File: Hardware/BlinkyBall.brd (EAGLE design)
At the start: 3 parts, among them IC3 TINY13-20SSU

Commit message: Adjust for LED
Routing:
- net S$13: track 1.59 -> 0.00 mm
- net S$11: track 19.2 -> 17.9 mm
- net S$8: track 0.63 -> 1.43 mm
- net S$6: track 0.79 -> 1.43 mm
- net S$2: track 5.71 -> 6.35 mm
- net N$28: track 8.24 -> 7.73 mm
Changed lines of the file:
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@@
 <text x="14.605" y="9.2075" size="1.6764" layer="1" rot="R90">9/12</text>
 <rectangle x1="7.77875" y1="15.5575" x2="10.31875" y2="18.0975" layer="1"/>
-<rectangle x1="11.58875" y1="5.08" x2="14.12875" y2="7.62" layer="1"/>
+<rectangle x1="11.58875" y1="5.23875" x2="14.12875" y2="7.6835" layer="1"/>
 <rectangle x1="11.58875" y1="16.1925" x2="14.605" y2="17.78" layer="1"/>
 <rectangle x1="11.58875" y1="14.12875" x2="14.605" y2="15.71625" layer="1"/>
 <text x="16.8275" y="11.7475" size="1.778" layer="1" rot="R90">SYN</text>
 <text x="18.7325" y="3.33375" size="1.778" layer="1" rot="R90">man</text>
-<text x="4.445" y="7.62" size="1.27" layer="1" rot="R270">blinky</text>
-<text x="7.62" y="4.445" size="1.27" layer="1" rot="R180">all</text>
-<text x="14.2875" y="4.445" size="1.016" layer="1" rot="R180">4.1</text>
+<text x="4.28625" y="8.09625" size="1.27" layer="1" rot="R270">blinky</text>
+<text x="7.3025" y="4.92125" size="1.27" layer="1" rot="R180">all</text>
+<text x="14.44625" y="4.60375" size="1.016" layer="1" rot="R180">4.1</text>
 <text x="18.25625" y="12.7" size="1.778" layer="1" rot="R90">shop</text>
-<text x="17.30375" y="2.2225" size="1.778" layer="1" rot="R90">data</text>
+<text x="17.30375" y="2.8575" size="1.778" layer="1" rot="R90">data</text>
 <text x="11.1125" y="10.63625" size="1.27" layer="1" rot="R180">Padi</text>
 <text x="11.43" y="9.36625" size="1.27" layer="1" rot="R180">wan</text>
@@
 <signal name="N$28">
 <contactref element="R3" pad="1"/>
-<wire x1="9.36625" y1="2.425" x2="9.2075" y2="2.54" width="0.4064" layer="1"/>
-<wire x1="9.2075" y1="2.54" x2="3.33375" y2="2.54" width="0.6096" layer="1"/>
-<wire x1="3.33375" y1="2.54" x2="3.33375" y2="4.715" width="0.6096" layer="1"/>
+<wire x1="9.36625" y1="3.01625" x2="3.33375" y2="3.01625" width="0.6096" layer="1"/>
+<wire x1="3.33375" y1="3.01625" x2="3.33375" y2="4.715" width="0.6096" layer="1"/>
 </signal>
 <signal name="N$30">
@@
 <wire x1="11.89625" y1="6.71225" x2="11.89625" y2="6.82625" width="0.4064" layer="1"/>
 <wire x1="11.89625" y1="6.82625" x2="11.90625" y2="6.82625" width="0.6096" layer="1"/>
-<wire x1="11.90625" y1="6.82625" x2="11.90625" y2="5.715" width="0.6096" layer="1"/>
+<wire x1="11.90625" y1="6.82625" x2="11.90625" y2="5.588" width="0.6096" layer="1"/>
 </signal>
 <signal name="N$15">
@@
 </signal>
 <signal name="S$2">
-<wire x1="10.63625" y1="4.445" x2="11.43" y2="4.445" width="0.6096" layer="1"/>
+<wire x1="10.63625" y1="4.445" x2="12.065" y2="4.445" width="0.6096" layer="1"/>
 <wire x1="9.36625" y1="17.78" x2="14.2875" y2="17.78" width="0.6096" layer="1"/>
 </signal>
@@
 <signal name="S$11">
 <wire x1="11.90625" y1="13.49375" x2="11.90625" y2="8.5725" width="0.6096" layer="1"/>
-<wire x1="15.08125" y1="8.5725" x2="15.08125" y2="2.54" width="0.6096" layer="1"/>
-<wire x1="15.08125" y1="2.54" x2="10.63625" y2="2.54" width="0.6096" layer="1"/>
+<wire x1="15.08125" y1="8.5725" x2="14.9225" y2="3.01625" width="0.6096" layer="1"/>
+<wire x1="14.9225" y1="3.01625" x2="11.27125" y2="3.01625" width="0.6096" layer="1"/>
 <wire x1="11.90625" y1="8.5725" x2="15.08125" y2="8.5725" width="0.6096" layer="1"/>
-<wire x1="10.63625" y1="2.54" x2="10.63625" y2="3.175" width="0.6096" layer="1"/>
+<wire x1="11.27125" y1="3.01625" x2="10.63625" y2="3.01625" width="0.6096" layer="1"/>
 </signal>
 <signal name="S$12">
@@
 </signal>
 <signal name="S$8">
-<wire x1="9.2075" y1="4.445" x2="8.5725" y2="4.445" width="0.6096" layer="1"/>
-</signal>
-<signal name="S$13">
-<wire x1="9.36625" y1="2.54" x2="9.36625" y2="3.33375" width="0.6096" layer="1"/>
-<wire x1="9.36625" y1="3.33375" x2="8.5725" y2="3.33375" width="0.6096" layer="1"/>
+<wire x1="9.2075" y1="4.445" x2="7.77875" y2="4.445" width="0.6096" layer="1"/>
 </signal>
 <signal name="S$1">
@@
 </signal>
 <signal name="S$6">
-<wire x1="10.63625" y1="3.33375" x2="11.43" y2="3.33375" width="0.6096" layer="1"/>
+<wire x1="10.63625" y1="3.01625" x2="12.065" y2="3.01625" width="0.6096" layer="1"/>
 </signal>
 <signal name="S$9">

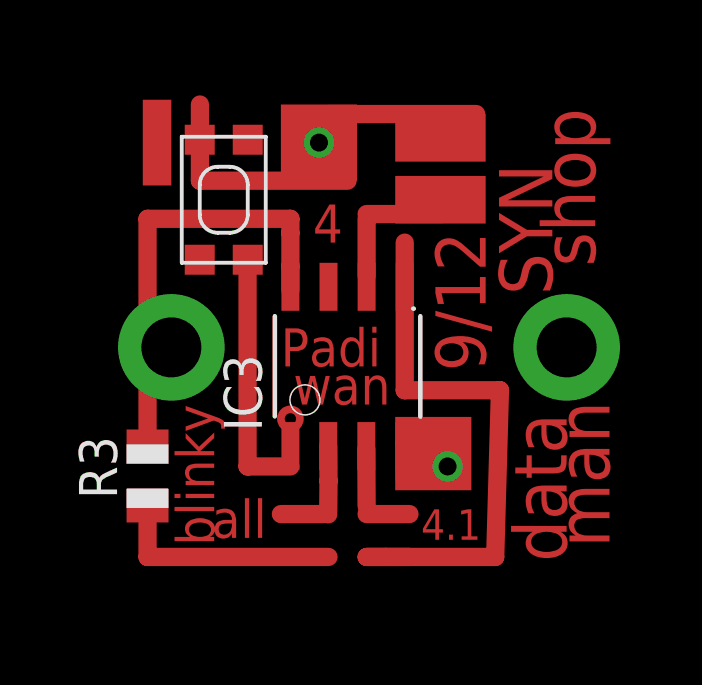
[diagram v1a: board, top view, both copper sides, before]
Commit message: Adjusting Layout, v4.2
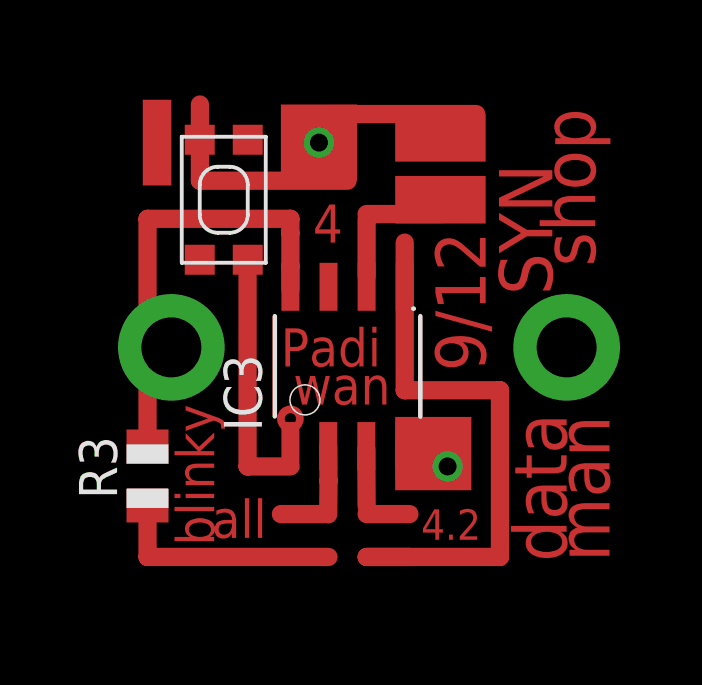
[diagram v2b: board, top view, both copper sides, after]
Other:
- board text added: "4.2"
- board text removed: "4.1"
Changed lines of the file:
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@@
 <rectangle x1="11.58875" y1="14.12875" x2="14.605" y2="15.71625" layer="1"/>
 <text x="16.8275" y="11.7475" size="1.778" layer="1" rot="R90">SYN</text>
-<text x="18.7325" y="3.33375" size="1.778" layer="1" rot="R90">man</text>
+<text x="18.7325" y="2.8575" size="1.778" layer="1" rot="R90">man</text>
 <text x="4.28625" y="8.09625" size="1.27" layer="1" rot="R270">blinky</text>
 <text x="7.3025" y="4.92125" size="1.27" layer="1" rot="R180">all</text>
-<text x="14.44625" y="4.60375" size="1.016" layer="1" rot="R180">4.1</text>
+<text x="14.44625" y="4.60375" size="1.016" layer="1" rot="R180">4.2</text>
 <text x="18.25625" y="12.7" size="1.778" layer="1" rot="R90">shop</text>
 <text x="17.30375" y="2.8575" size="1.778" layer="1" rot="R90">data</text>
@@
 <signal name="S$11">
 <wire x1="11.90625" y1="13.49375" x2="11.90625" y2="8.5725" width="0.6096" layer="1"/>
-<wire x1="15.08125" y1="8.5725" x2="14.9225" y2="3.01625" width="0.6096" layer="1"/>
-<wire x1="14.9225" y1="3.01625" x2="11.27125" y2="3.01625" width="0.6096" layer="1"/>
+<wire x1="15.08125" y1="8.5725" x2="15.08125" y2="3.01625" width="0.6096" layer="1"/>
+<wire x1="15.08125" y1="3.01625" x2="10.63625" y2="3.01625" width="0.6096" layer="1"/>
 <wire x1="11.90625" y1="8.5725" x2="15.08125" y2="8.5725" width="0.6096" layer="1"/>
-<wire x1="11.27125" y1="3.01625" x2="10.63625" y2="3.01625" width="0.6096" layer="1"/>
 </signal>
 <signal name="S$12">

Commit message: Final Board Adjustments?
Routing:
- net S$2: track 6.35 -> 8.73 mm
- net S$5: track 2.54 -> 4.29 mm
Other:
- board text added: "4.3"
- board text added: "hop"
- board text removed: "4"
- board text removed: "4.2"
- board text removed: "shop"
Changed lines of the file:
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@@
 <plain>
 <circle x="8.09625" y="7.62" radius="0.3175" width="0.254" layer="1"/>
-<text x="14.605" y="9.2075" size="1.6764" layer="1" rot="R90">9/12</text>
 <rectangle x1="7.77875" y1="15.5575" x2="10.31875" y2="18.0975" layer="1"/>
 <rectangle x1="11.58875" y1="5.23875" x2="14.12875" y2="7.6835" layer="1"/>
-<rectangle x1="11.58875" y1="16.1925" x2="14.605" y2="17.78" layer="1"/>
-<rectangle x1="11.58875" y1="14.12875" x2="14.605" y2="15.71625" layer="1"/>
-<text x="16.8275" y="11.7475" size="1.778" layer="1" rot="R90">SYN</text>
 <text x="18.7325" y="2.8575" size="1.778" layer="1" rot="R90">man</text>
-<text x="4.28625" y="8.09625" size="1.27" layer="1" rot="R270">blinky</text>
-<text x="7.3025" y="4.92125" size="1.27" layer="1" rot="R180">all</text>
-<text x="14.44625" y="4.60375" size="1.016" layer="1" rot="R180">4.2</text>
-<text x="18.25625" y="12.7" size="1.778" layer="1" rot="R90">shop</text>
+<text x="4.445" y="7.3025" size="1.016" layer="1" rot="R270">blinky</text>
+<text x="6.985" y="4.7625" size="1.016" layer="1" rot="R180">all</text>
+<text x="13.81125" y="16.8275" size="1.4224" layer="1" rot="R180">4.3</text>
 <text x="17.30375" y="2.8575" size="1.778" layer="1" rot="R90">data</text>
-<text x="11.1125" y="10.63625" size="1.27" layer="1" rot="R180">Padi</text>
-<text x="11.43" y="9.36625" size="1.27" layer="1" rot="R180">wan</text>
-<text x="9.8425" y="14.76375" size="1.27" layer="1" rot="R180">4</text>
+<text x="10.95375" y="10.795" size="1.27" layer="1" rot="R180">Padi</text>
+<text x="11.27125" y="9.525" size="1.27" layer="1" rot="R180">wan</text>
 <rectangle x1="3.175" y1="15.39875" x2="4.1275" y2="18.25625" layer="1"/>
+<rectangle x1="14.44625" y1="16.1925" x2="18.89125" y2="18.0975" layer="1"/>
+<text x="13.97" y="13.49375" size="1.27" layer="1" rot="SR270">SYN</text>
+<text x="15.5575" y="12.3825" size="1.27" layer="1">hop</text>
+<text x="12.54125" y="12.85875" size="1.016" layer="1" rot="R270">9/12</text>
+<rectangle x1="14.44625" y1="14.12875" x2="18.89125" y2="15.24" layer="1"/>
 </plain>
 <attributes>
@@
 <contactref element="IC3" pad="3"/>
 <wire x1="10.62625" y1="6.71225" x2="10.62625" y2="6.61375" width="0.4064" layer="1"/>
-<wire x1="10.62625" y1="6.61375" x2="10.63625" y2="4.71875" width="0.6096" layer="1"/>
+<wire x1="10.62625" y1="6.61375" x2="10.63625" y2="4.40125" width="0.6096" layer="1"/>
 </signal>
 <signal name="N$28">
@@
 </signal>
 <signal name="S$2">
-<wire x1="10.63625" y1="4.445" x2="12.065" y2="4.445" width="0.6096" layer="1"/>
-<wire x1="9.36625" y1="17.78" x2="14.2875" y2="17.78" width="0.6096" layer="1"/>
+<wire x1="10.63625" y1="4.445" x2="13.97" y2="4.445" width="0.6096" layer="1"/>
+<wire x1="9.36625" y1="17.78" x2="14.76375" y2="17.78" width="0.6096" layer="1"/>
 </signal>
 <signal name="S$3">
@@
 </signal>
 <signal name="S$5">
-<wire x1="10.63625" y1="14.44625" x2="13.17625" y2="14.44625" width="0.6096" layer="1"/>
+<wire x1="10.63625" y1="14.44625" x2="14.9225" y2="14.44625" width="0.6096" layer="1"/>
 </signal>
 <signal name="S$6">
